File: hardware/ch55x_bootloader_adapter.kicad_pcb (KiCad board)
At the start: 2 copper layers, 44.3 x 13 mm, 7 parts

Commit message: update adapter pcb
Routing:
- net /USB_DP: track 0.00 -> 50.6 mm, vias 0 -> 2
- net /USB_DN: track 0.00 -> 38.8 mm, vias 0 -> 2
- net /CC2: track 0.00 -> 37.0 mm, vias 0 -> 3
- net /CC1: track 0.00 -> 36.7 mm, vias 0 -> 2
- net /SBU1: track 0.00 -> 36.4 mm, vias 0 -> 2
- net /SBU2: track 0.00 -> 36.3 mm, vias 0 -> 3
- net /GND: track 0.00 -> 13.3 mm
- net /VBUS_SW: track 36.8 -> 43.6 mm
- net (no net): track 1.25 -> 0.00 mm
- added copper zone on B.Cu, net /VBUS_SW
- added copper zone on F.Cu, net /VBUS_SW

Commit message: more hardware progress
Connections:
- USB_C_PLUG1 pad A8: /SBU1 -> unconnected-(USB_C_PLUG1-SBU1-PadA8)
- USB_C_PLUG1 pad B8: /SBU2 -> unconnected-(USB_C_PLUG1-SBU2-PadB8)
- USB_C_RECEPTABLE1 pad A8: /SBU1 -> unconnected-(USB_C_RECEPTABLE1-SBU1-PadA8)
- USB_C_RECEPTABLE1 pad B8: /SBU2 -> unconnected-(USB_C_RECEPTABLE1-SBU2-PadB8)
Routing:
- net /GND: track 13.3 -> 52.9 mm, vias 0 -> 9
- net /SBU1: track 36.4 -> 0.00 mm, vias 2 -> 0
- net /SBU2: track 36.3 -> 0.00 mm, vias 3 -> 0
- net /VBUS_SW: track 43.6 -> 46.5 mm, vias 0 -> 2

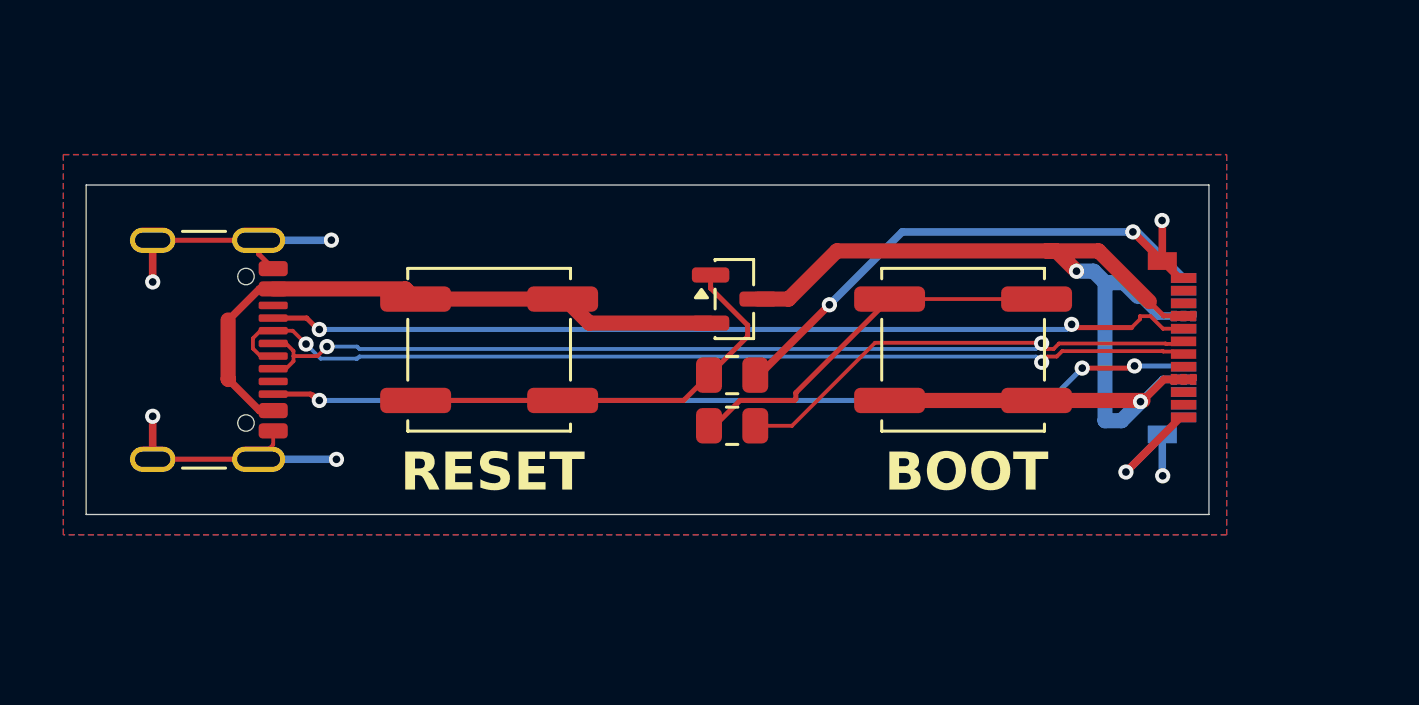
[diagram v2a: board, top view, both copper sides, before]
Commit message: change adapter to be USB-A instead for simplicity and cost
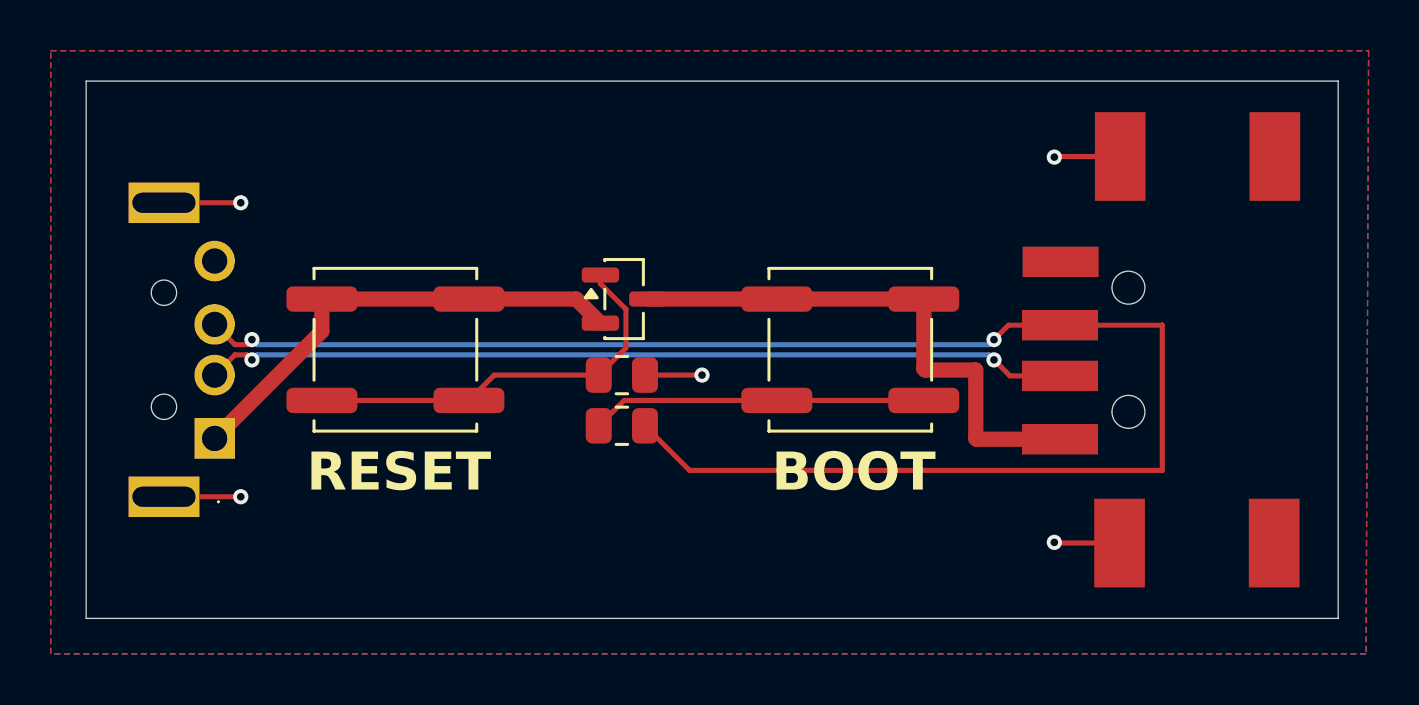
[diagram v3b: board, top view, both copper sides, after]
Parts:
- removed USB_C_PLUG1: USB_C_Plug_Molex_105444, Connector_USB:USB_C_Plug_Molex_105444
- removed USB_C_RECEPTABLE1: USB_C_Receptacle_USB2.0_14P, Connector_USB:USB_C_Receptacle_GCT_USB4105-xx-A_16P_TopMnt_Horizontal
- added U1: USB-A MALE, jlc:USB-A-TH_U-G-04WD-W-01, F.Cu at (90.3, 61.5)
- added USB1: USB-A FEMALE, jlc:USB-A-SMD_U-A-24SS-W-2, F.Cu at (128.9, 61.5)
- BOOT1: value SW_Push -> BOOT_SW
- RESET1: value SW_Push -> RESET_SW
- RESET_MOSFET1: value Q_PMOS_GSD -> PWR_MOSFET
- moved BOOT1 4.45 mm to (116.3, 61.5)
- moved RESET_MOSFET1 4.35 mm to (107.4, 59.5)
- moved BOOT_R1 4.35 mm to (107.3, 64.5)
- moved RESET_R1 4.35 mm to (107.3, 62.5)
- moved RESET1 3.70 mm to (98.4, 61.5)
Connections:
- net /VBUS_IN renamed /VCC_IN
- BOOT1 pad 1: Net-(BOOT1-Pad1) -> /VCC_OUT
- BOOT1 pad 2: /VBUS_SW -> Net-(BOOT1-Pad2)
- BOOT_R1 pad 1: Net-(BOOT1-Pad1) -> Net-(BOOT1-Pad2)
- RESET_MOSFET1 pad 3: /VBUS_SW -> /VCC_OUT
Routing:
- net /VBUS_SW: track 46.5 -> 0.00 mm, vias 2 -> 0
- net /GND: track 52.9 -> 13.5 mm, vias 9 -> 5
- net /CC2: track 37.0 -> 0.00 mm, vias 3 -> 0
- net /CC1: track 36.7 -> 0.00 mm, vias 2 -> 0
- net /VCC_OUT: track 0.00 -> 21.7 mm
- net Net-(BOOT1-Pad1): track 15.1 -> 0.00 mm
- net /USB_DP: track 50.6 -> 65.1 mm
- net Net-(BOOT1-Pad2): track 0.00 -> 13.2 mm
- net /VCC_IN: track 24.7 -> 18.6 mm
- net /USB_DN: track 39.0 -> 34.2 mm
- net Net-(RESET_MOSFET1-G): track 17.2 -> 16.2 mm
- removed copper zone on B.Cu, net /VBUS_SW
- removed copper zone on F.Cu, net /VBUS_SW
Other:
- board size 44.3 x 13 mm -> 49.4 x 21.2 mm

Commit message: swap to new buttons and improve layout further
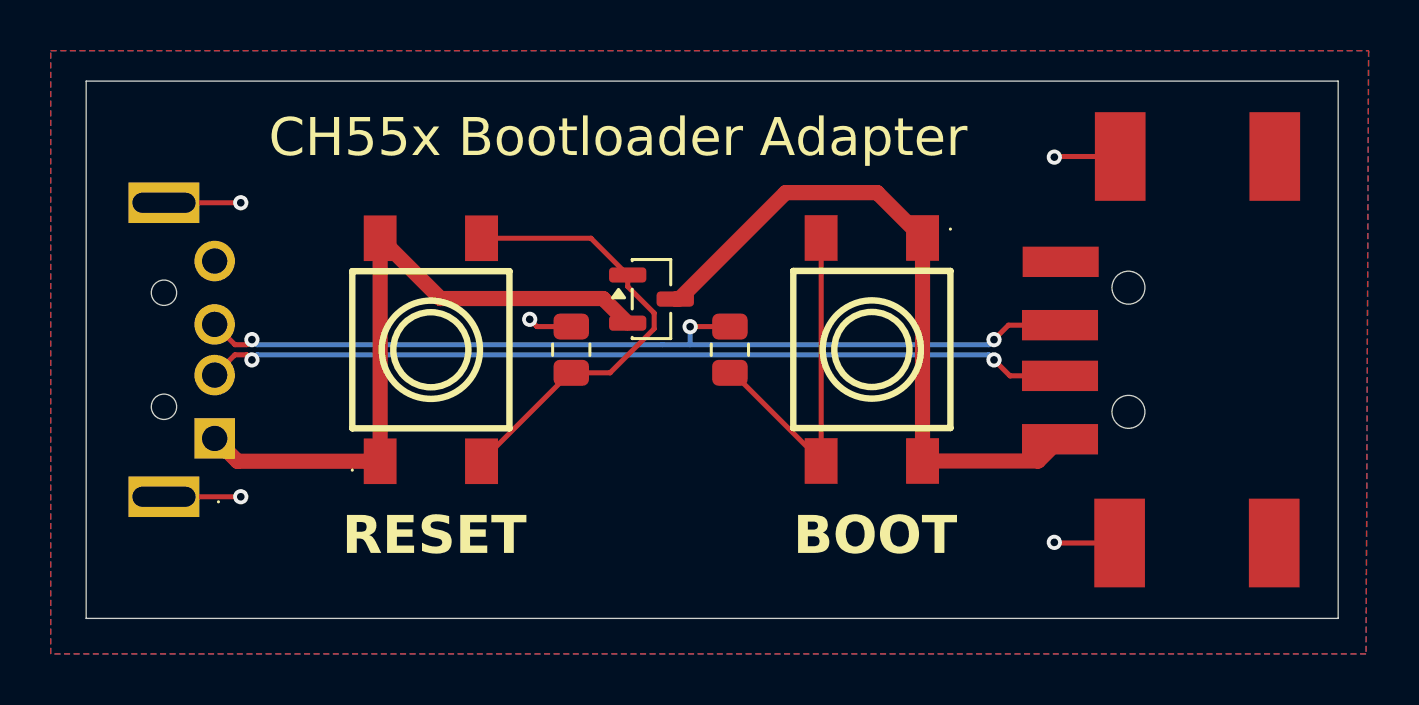
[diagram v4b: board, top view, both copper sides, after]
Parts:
- BOOT1, RESET1: footprint Button_Switch_SMD:SW_Push_1P1T_NO_CK_KSC7xxJ -> jlc:SW-SMD_4P-L6.2-W6.2-P4.00-LS9.5-TL
- moved BOOT_R1 5.21 mm to (111.6, 61.5), turned to 90 degrees
- moved RESET_R1 2.23 mm to (105.3, 61.5), turned to 90 degrees
- moved RESET1 1.40 mm to (99.8, 61.5), turned to 90 degrees
- moved RESET_MOSFET1 1.08 mm to (108.5, 59.5)
- moved BOOT1 0.85 mm to (117.2, 61.5), turned to -90 degrees
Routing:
- net /USB_DP: track 65.1 -> 36.6 mm, vias 2 -> 3
- net /VCC_IN: track 18.6 -> 26.9 mm
- net /VCC_OUT: track 21.7 -> 26.8 mm
- net Net-(RESET_MOSFET1-G): track 16.2 -> 17.9 mm
- net Net-(BOOT1-Pad2): track 13.2 -> 13.8 mm
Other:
- board text added: "CH55x Bootloader Adapter"
